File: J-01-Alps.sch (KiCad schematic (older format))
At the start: 3 parts, among them U1 ATmega32U4-AU

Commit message: Another attempt at adding more libraries
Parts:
- C5: renamed from C?; value C_Small -> 1uF; footprint (none) -> Capacitor_SMD:C_0603_1608Metric_Pad1.08x0.95mm_HandSolder
- R6: footprint Resistor_SMD:R_0402_1005Metric_Pad0.72x0.64mm_HandSolder -> Resistor_SMD:R_0603_1608Metric_Pad0.98x0.95mm_HandSolder
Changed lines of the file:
@@
 F 0 "R6" V 6454 3750 50  0000 C CNN
 F 1 "10k" V 6545 3750 50  0000 C CNN
-F 2 "Resistor_SMD:R_0402_1005Metric_Pad0.72x0.64mm_HandSolder" H 6650 3750 50  0001 C CNN
+F 2 "Resistor_SMD:R_0603_1608Metric_Pad0.98x0.95mm_HandSolder" H 6650 3750 50  0001 C CNN
 F 3 "~" H 6650 3750 50  0001 C CNN
 	1    6650 3750
@@
 	5400 4950 5500 4950
 $Comp
-L Device:C_Small C?
+L Device:C_Small C5
 U 1 1 61BC454C
 P 4200 3050
-F 0 "C?" H 4292 3096 50  0000 L CNN
-F 1 "C_Small" H 4292 3005 50  0000 L CNN
-F 2 "" H 4200 3050 50  0001 C CNN
+F 0 "C5" H 4292 3096 50  0000 L CNN
+F 1 "1uF" H 4292 3005 50  0000 L CNN
+F 2 "Capacitor_SMD:C_0603_1608Metric_Pad1.08x0.95mm_HandSolder" H 4200 3050 50  0001 C CNN
 F 3 "~" H 4200 3050 50  0001 C CNN
 	1    4200 3050

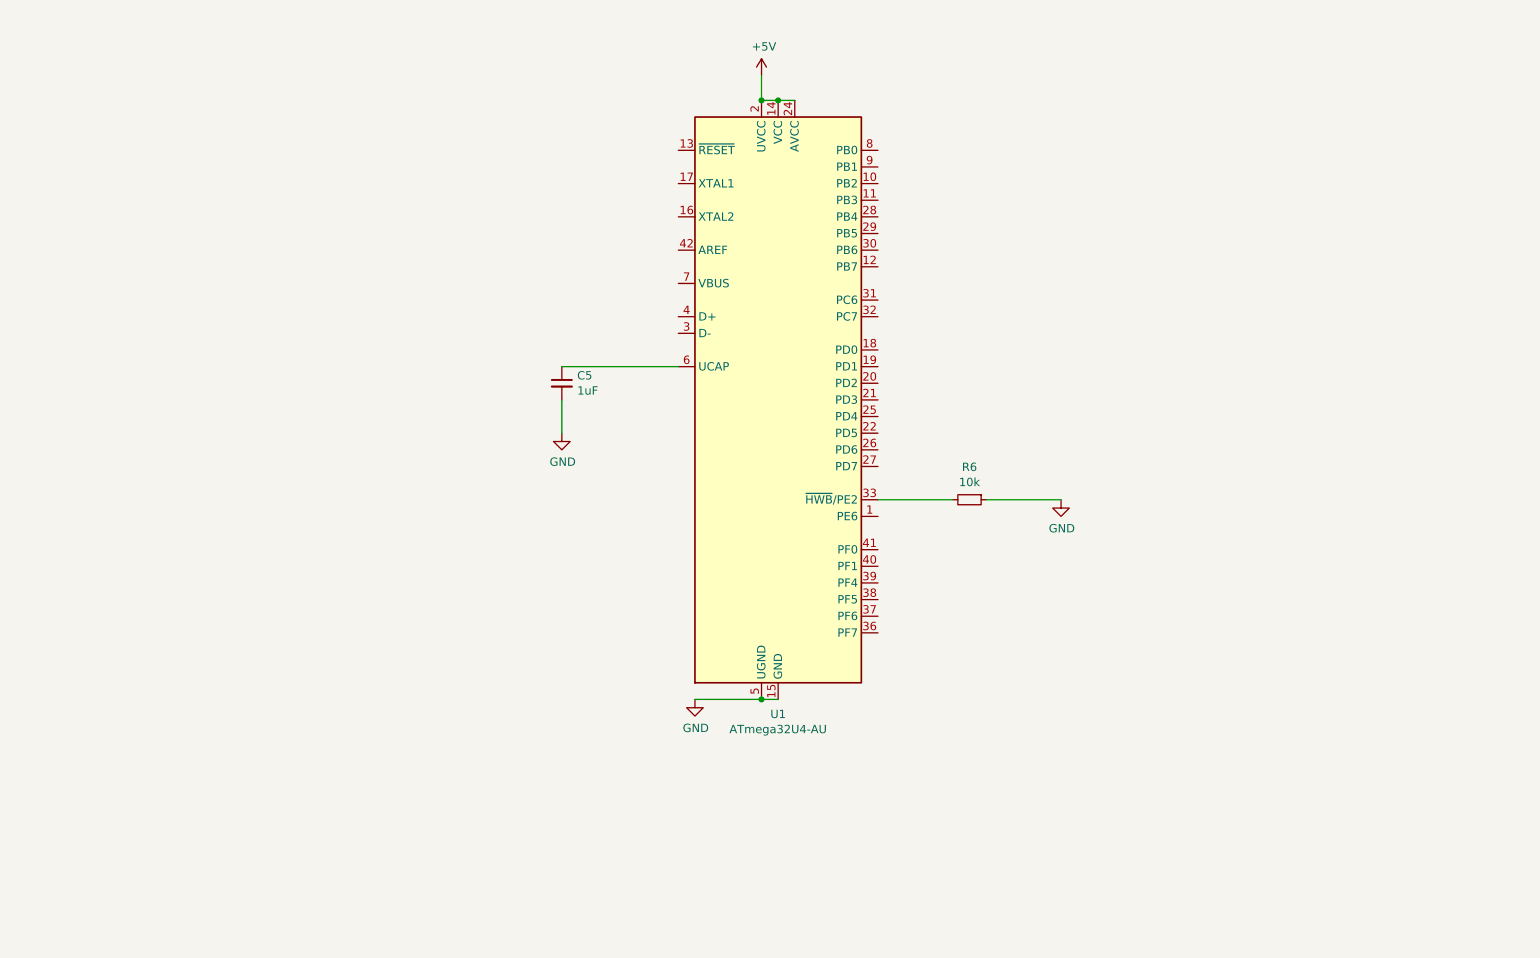
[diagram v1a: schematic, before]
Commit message: MCU and Matrix Layout
Continued work on the MCU component layout and the switch matrix.
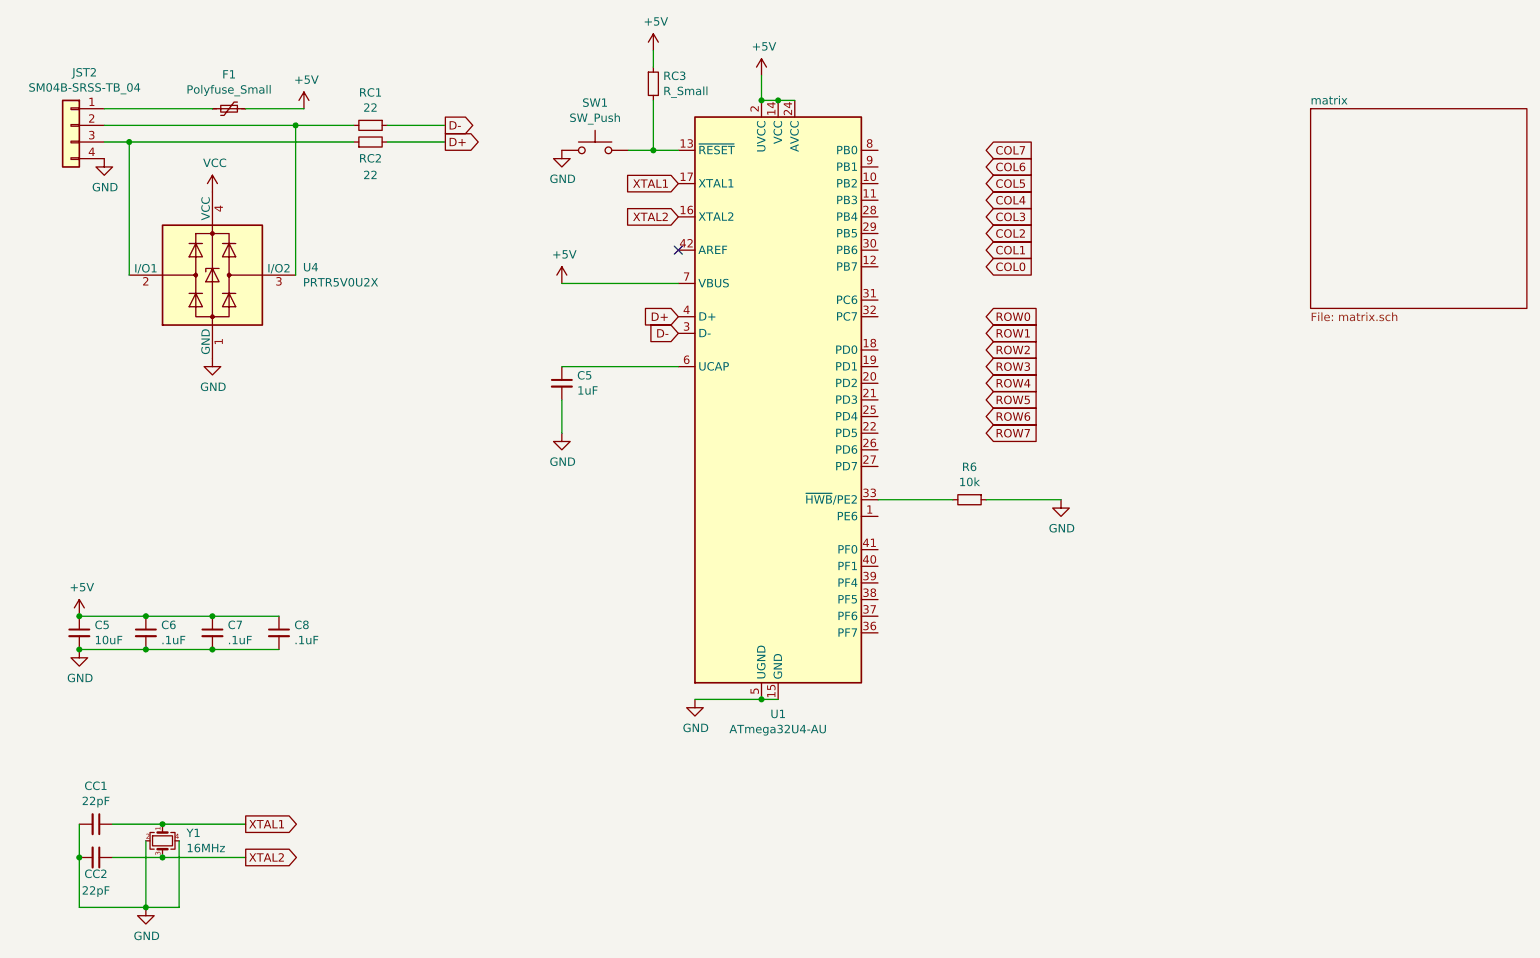
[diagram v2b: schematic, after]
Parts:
- added C5: 10uF, Capacitor_SMD:C_0603_1608Metric_Pad1.08x0.95mm_HandSolder, symbol Device:C_Small
- added C6, C7, C8: .1uF, Capacitor_SMD:C_0603_1608Metric_Pad1.08x0.95mm_HandSolder, symbol Device:C_Small
- added CC1, CC2: 22pF, Capacitor_SMD:C_0603_1608Metric_Pad1.08x0.95mm_HandSolder, symbol Device:C_Small
- added F1: Polyfuse_Small, Fuse:Fuse_1206_3216Metric_Pad1.42x1.75mm_HandSolder, symbol Device:Polyfuse_Small
- added JST2: SM04B-SRSS-TB_04, Connector_JST:JST_SH_SM04B-SRSS-TB_1x04-1MP_P1.00mm_Horizontal, symbol Connector_Generic:Conn_01x04
- added RC1, RC2: 22, Resistor_SMD:R_0603_1608Metric_Pad0.98x0.95mm_HandSolder, symbol Device:R_Small
- added RC3: R_Small, Resistor_SMD:R_0603_1608Metric_Pad0.98x0.95mm_HandSolder, symbol Device:R_Small
- added SW1: SW_Push, random-keyboard-parts:SKQGADE010, symbol Switch:SW_Push
- added U4: PRTR5V0U2X, Package_TO_SOT_SMD:SOT-143, symbol Power_Protection:PRTR5V0U2X
- added Y1: 16MHz, Crystal:Crystal_SMD_3225-4Pin_3.2x2.5mm_HandSoldering, symbol Device:Crystal_GND24_Small
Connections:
- net +5V: now also U1.7 (VBUS), C5.1, C6.1, C7.1, C8.1, F1.1, RC3.1
- net GND: now also C5.2, C6.2, C7.2, C8.2, CC1.2, CC2.2, JST2.4 (Pin_4), SW1.1, U4.1 (GND), Y1.2, Y1.4
- net at U1.13 (~RESET): now also RC3.2, SW1.2
- net XTAL2: now reaches U1.16 (XTAL2)
- net XTAL2: now also CC2.1, Y1.3
- net XTAL1: now reaches U1.17 (XTAL1)
- net XTAL1: now also CC1.1, Y1.1
- net D-: now reaches U1.3 (D-)
- net D-: now also RC1.1
- net D+: now reaches U1.4 (D+)
- net D+: now also RC2.2
- new net: F1.2, JST2.1 (Pin_1)
- new net: JST2.2 (Pin_2), RC1.2, U4.3 (I/O2)
- new net: JST2.3 (Pin_3), RC2.1, U4.2 (I/O1)
- new net VCC: U4.4 (VCC)
- no-connect marks 0 -> 1

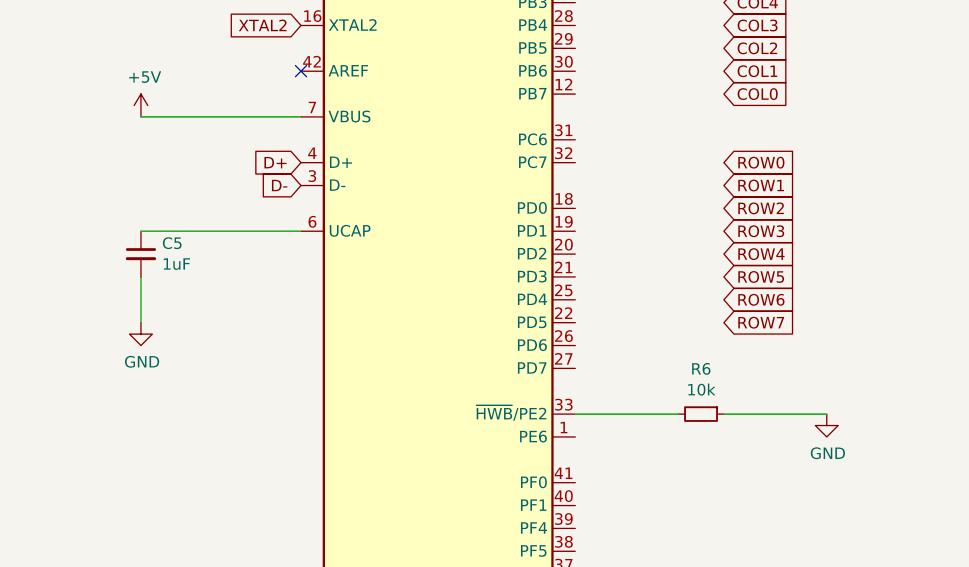
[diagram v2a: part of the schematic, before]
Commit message: Matrix Draft complete
First draft of the switch matrix is complete.
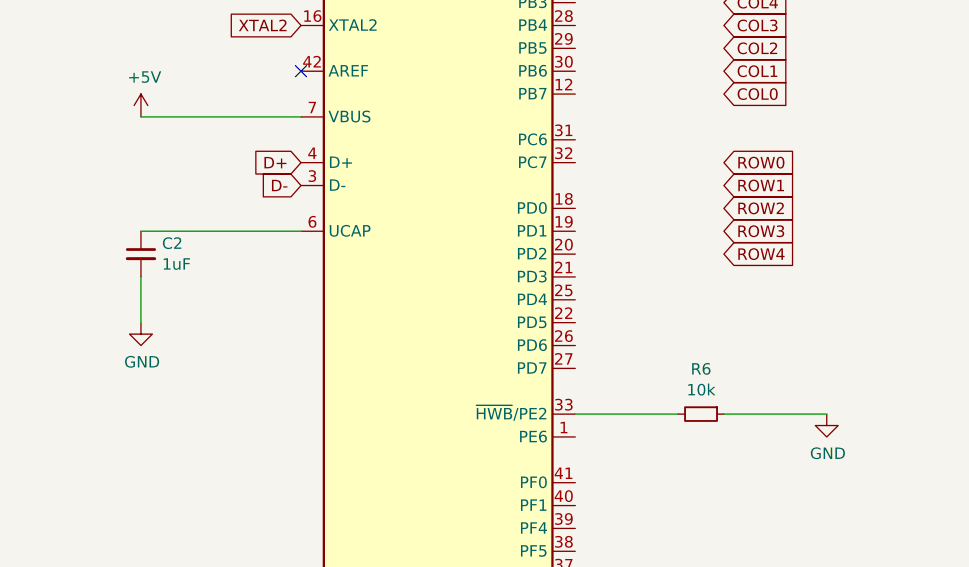
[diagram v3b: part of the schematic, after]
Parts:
- renumbered C5 to C2
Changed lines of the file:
@@
 $EndComp
 $Comp
-L power:+5V #PWR?
+L power:+5V #PWR0101
 U 1 1 61BC16E3
 P 5400 1200
-F 0 "#PWR?" H 5400 1050 50  0001 C CNN
+F 0 "#PWR0101" H 5400 1050 50  0001 C CNN
 F 1 "+5V" H 5415 1373 50  0000 C CNN
 F 2 "" H 5400 1200 50  0001 C CNN
@@
 	6100 3750 6550 3750
 $Comp
-L power:GND #PWR?
+L power:GND #PWR0102
 U 1 1 61BC3609
 P 7200 3750
-F 0 "#PWR?" H 7200 3500 50  0001 C CNN
+F 0 "#PWR0102" H 7200 3500 50  0001 C CNN
 F 1 "GND" H 7205 3577 50  0000 C CNN
 F 2 "" H 7200 3750 50  0001 C CNN
@@
 	6750 3750 7200 3750
 $Comp
-L power:GND #PWR?
+L power:GND #PWR0103
 U 1 1 61BC3DB0
 P 5000 4950
-F 0 "#PWR?" H 5000 4700 50  0001 C CNN
+F 0 "#PWR0103" H 5000 4700 50  0001 C CNN
 F 1 "GND" H 5005 4777 50  0000 C CNN
 F 2 "" H 5000 4950 50  0001 C CNN
@@
 	5400 4950 5500 4950
 $Comp
-L Device:C_Small C5
+L Device:C_Small C2
 U 1 1 61BC454C
 P 4200 3050
-F 0 "C5" H 4292 3096 50  0000 L CNN
+F 0 "C2" H 4292 3096 50  0000 L CNN
 F 1 "1uF" H 4292 3005 50  0000 L CNN
 F 2 "Capacitor_SMD:C_0603_1608Metric_Pad1.08x0.95mm_HandSolder" H 4200 3050 50  0001 C CNN
@@
 	4200 2950 4900 2950
 $Comp
-L power:GND #PWR?
+L power:GND #PWR0104
 U 1 1 61BC5372
 P 4200 3350
-F 0 "#PWR?" H 4200 3100 50  0001 C CNN
+F 0 "#PWR0104" H 4200 3100 50  0001 C CNN
 F 1 "GND" H 4205 3177 50  0000 C CNN
 F 2 "" H 4200 3350 50  0001 C CNN
@@
 D-
 $Comp
-L power:+5V #PWR?
+L power:+5V #PWR0105
 U 1 1 61BD316B
 P 4200 2450
-F 0 "#PWR?" H 4200 2300 50  0001 C CNN
+F 0 "#PWR0105" H 4200 2300 50  0001 C CNN
 F 1 "+5V" H 4215 2623 50  0000 C CNN
 F 2 "" H 4200 2450 50  0001 C CNN
@@
 $EndComp
 $Comp
-L power:GND #PWR?
+L power:GND #PWR0106
 U 1 1 61BD5C0D
 P 4200 1650
-F 0 "#PWR?" H 4200 1400 50  0001 C CNN
+F 0 "#PWR0106" H 4200 1400 50  0001 C CNN
 F 1 "GND" H 4205 1477 50  0000 C CNN
 F 2 "" H 4200 1650 50  0001 C CNN
@@
 	4750 1650 4900 1650
 $Comp
-L power:+5V #PWR?
+L power:+5V #PWR0107
 U 1 1 61BD7131
 P 4750 1050
-F 0 "#PWR?" H 4750 900 50  0001 C CNN
+F 0 "#PWR0107" H 4750 900 50  0001 C CNN
 F 1 "+5V" H 4765 1223 50  0000 C CNN
 F 2 "" H 4750 1050 50  0001 C CNN
@@
 $EndComp
 $Comp
-L power:GND #PWR?
+L power:GND #PWR0108
 U 1 1 61BDB16D
 P 1700 6200
-F 0 "#PWR?" H 1700 5950 50  0001 C CNN
+F 0 "#PWR0108" H 1700 5950 50  0001 C CNN
 F 1 "GND" H 1705 6027 50  0000 C CNN
 F 2 "" H 1700 6200 50  0001 C CNN
@@
 $EndComp
 $Comp
-L power:+5V #PWR?
+L power:+5V #PWR0109
 U 1 1 61BDFF00
 P 1300 4450
-F 0 "#PWR?" H 1300 4300 50  0001 C CNN
+F 0 "#PWR0109" H 1300 4300 50  0001 C CNN
 F 1 "+5V" H 1315 4623 50  0000 C CNN
 F 2 "" H 1300 4450 50  0001 C CNN
@@
 $EndComp
 $Comp
-L power:GND #PWR?
+L power:GND #PWR0110
 U 1 1 61BE07B1
 P 1300 4650
-F 0 "#PWR?" H 1300 4400 50  0001 C CNN
+F 0 "#PWR0110" H 1300 4400 50  0001 C CNN
 F 1 "GND" H 1305 4477 50  0000 C CNN
 F 2 "" H 1300 4650 50  0001 C CNN
@@
 	2100 4450 2500 4450
 $Comp
-L power:+5V #PWR?
+L power:+5V #PWR0111
 U 1 1 61BE4541
 P 2650 1400
-F 0 "#PWR?" H 2650 1250 50  0001 C CNN
+F 0 "#PWR0111" H 2650 1250 50  0001 C CNN
 F 1 "+5V" H 2665 1573 50  0000 C CNN
 F 2 "" H 2650 1400 50  0001 C CNN
@@
 	1450 1500 2600 1500
 $Comp
-L power:GND #PWR?
+L power:GND #PWR0112
 U 1 1 61BE8603
 P 1450 1700
-F 0 "#PWR?" H 1450 1450 50  0001 C CNN
+F 0 "#PWR0112" H 1450 1450 50  0001 C CNN
 F 1 "GND" H 1455 1527 50  0000 C CNN
 F 2 "" H 1450 1700 50  0001 C CNN
@@
 $EndComp
 $Comp
-L power:GND #PWR?
+L power:GND #PWR0113
 U 1 1 61BE9C36
 P 2100 2900
-F 0 "#PWR?" H 2100 2650 50  0001 C CNN
+F 0 "#PWR0113" H 2100 2650 50  0001 C CNN
 F 1 "GND" H 2105 2727 50  0000 C CNN
 F 2 "" H 2100 2900 50  0001 C CNN
@@
 	2600 1500 2950 1500
 $Comp
-L power:VCC #PWR?
+L power:VCC #PWR0114
 U 1 1 61BEE6C5
 P 2100 1900
-F 0 "#PWR?" H 2100 1750 50  0001 C CNN
+F 0 "#PWR0114" H 2100 1750 50  0001 C CNN
 F 1 "VCC" H 2115 2073 50  0000 C CNN
 F 2 "" H 2100 1900 50  0001 C CNN
@@
 Text GLabel 6750 3050 2    50   Input ~ 0
 ROW4
-Text GLabel 6750 3150 2    50   Input ~ 0
-ROW5
-Text GLabel 6750 3250 2    50   Input ~ 0
-ROW6
-Text GLabel 6750 3350 2    50   Input ~ 0
-ROW7
 Text GLabel 6750 2350 2    50   Input ~ 0
 COL0

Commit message: Bugfixes
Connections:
- net COL0: now also U1.9 (PB1)
- net COL1: now also U1.41 (PF0)
- net COL2: now also U1.36 (PF7)
- net COL3: now also U1.40 (PF1)
- net COL4: now also U1.39 (PF4)
- net COL5: now also U1.32 (PC7)
- net COL6: now also U1.31 (PC6)
- net COL7: now also U1.30 (PB6)
- net ROW0: now also U1.11 (PB3)
- net ROW1: now also U1.10 (PB2)
- net ROW2: now also U1.8 (PB0)
- net ROW3: now also U1.37 (PF6)
- net ROW4: now also U1.38 (PF5)
- net VCC: now also F1.2, JST2.1 (Pin_1)
- net COL17: now reaches U1.18 (PD0)
- net COL16: now reaches U1.19 (PD1)
- net COL15: now reaches U1.20 (PD2)
- net COL14: now reaches U1.21 (PD3)
- net COL13: now reaches U1.22 (PD5)
- net COL12: now reaches U1.25 (PD4)
- net COL11: now reaches U1.26 (PD6)
- net COL10: now reaches U1.27 (PD7)
- net COL9: now reaches U1.28 (PB4)
- net COL8: now reaches U1.29 (PB5)
- no-connect marks 1 -> 3
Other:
- moved on the sheet: F1, RC1, RC2
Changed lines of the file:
@@
 L power:GND #PWR0104
 U 1 1 61BC5372
-P 4200 3350
-F 0 "#PWR0104" H 4200 3100 50  0001 C CNN
-F 1 "GND" H 4205 3177 50  0000 C CNN
-F 2 "" H 4200 3350 50  0001 C CNN
-F 3 "" H 4200 3350 50  0001 C CNN
-	1    4200 3350
-	1    0    0    -1
-$EndComp
-Wire Wire Line
-	4200 3350 4200 3150
+P 4200 3300
+F 0 "#PWR0104" H 4200 3050 50  0001 C CNN
+F 1 "GND" H 4205 3127 50  0000 C CNN
+F 2 "" H 4200 3300 50  0001 C CNN
+F 3 "" H 4200 3300 50  0001 C CNN
+	1    4200 3300
+	1    0    0    -1
+$EndComp
 $Comp
 L Connector_Generic:Conn_01x04 JST2
@@
 L Device:Polyfuse_Small F1
 U 1 1 61BC3615
-P 2200 1400
-F 0 "F1" V 1995 1400 50  0000 C CNN
-F 1 "Polyfuse_Small" V 2086 1400 50  0000 C CNN
-F 2 "Fuse:Fuse_1206_3216Metric_Pad1.42x1.75mm_HandSolder" H 2250 1200 50  0001 L CNN
-F 3 "~" H 2200 1400 50  0001 C CNN
-	1    2200 1400
+P 1750 3700
+F 0 "F1" V 1545 3700 50  0000 C CNN
+F 1 "Polyfuse_Small" V 1636 3700 50  0000 C CNN
+F 2 "Fuse:Fuse_1206_3216Metric_Pad1.42x1.75mm_HandSolder" H 1800 3500 50  0001 L CNN
+F 3 "~" H 1750 3700 50  0001 C CNN
+	1    1750 3700
 	0    1    1    0
 $EndComp
@@
 L Device:R_Small RC1
 U 1 1 61BC52CD
-P 3050 1500
-F 0 "RC1" V 2854 1500 50  0000 C CNN
-F 1 "22" V 2945 1500 50  0000 C CNN
-F 2 "Resistor_SMD:R_0603_1608Metric_Pad0.98x0.95mm_HandSolder" H 3050 1500 50  0001 C CNN
-F 3 "~" H 3050 1500 50  0001 C CNN
-	1    3050 1500
+P 3000 1500
+F 0 "RC1" V 2804 1500 50  0000 C CNN
+F 1 "22" V 2895 1500 50  0000 C CNN
+F 2 "Resistor_SMD:R_0603_1608Metric_Pad0.98x0.95mm_HandSolder" H 3000 1500 50  0001 C CNN
+F 3 "~" H 3000 1500 50  0001 C CNN
+	1    3000 1500
 	0    1    1    0
 $EndComp
@@
 L Device:R_Small RC2
 U 1 1 61BC5632
-P 3050 1600
-F 0 "RC2" V 2950 1600 50  0000 C CNN
-F 1 "22" V 2850 1600 50  0000 C CNN
-F 2 "Resistor_SMD:R_0603_1608Metric_Pad0.98x0.95mm_HandSolder" H 3050 1600 50  0001 C CNN
-F 3 "~" H 3050 1600 50  0001 C CNN
-	1    3050 1600
+P 3000 1600
+F 0 "RC2" V 2900 1600 50  0000 C CNN
+F 1 "22" V 2800 1600 50  0000 C CNN
+F 2 "Resistor_SMD:R_0603_1608Metric_Pad0.98x0.95mm_HandSolder" H 3000 1600 50  0001 C CNN
+F 3 "~" H 3000 1600 50  0001 C CNN
+	1    3000 1600
 	0    -1   -1   0
 $EndComp
-Text GLabel 3500 1500 2    50   Output ~ 0
+Text GLabel 3300 1500 2    50   Output ~ 0
 D-
-Text GLabel 3500 1600 2    50   Output ~ 0
+Text GLabel 3300 1600 2    50   Output ~ 0
 D+
 Wire Wire Line
-	3150 1500 3500 1500
-Wire Wire Line
-	3150 1600 3500 1600
+	3100 1500 3300 1500
+Wire Wire Line
+	3100 1600 3300 1600
 Text GLabel 4900 2650 0    50   Input ~ 0
 D+
@@
 L power:+5V #PWR0111
 U 1 1 61BE4541
-P 2650 1400
-F 0 "#PWR0111" H 2650 1250 50  0001 C CNN
-F 1 "+5V" H 2665 1573 50  0000 C CNN
-F 2 "" H 2650 1400 50  0001 C CNN
-F 3 "" H 2650 1400 50  0001 C CNN
-	1    2650 1400
-	1    0    0    -1
-$EndComp
-Wire Wire Line
-	2300 1400 2650 1400
+P 2150 3700
+F 0 "#PWR0111" H 2150 3550 50  0001 C CNN
+F 1 "+5V" H 2165 3873 50  0000 C CNN
+F 2 "" H 2150 3700 50  0001 C CNN
+F 3 "" H 2150 3700 50  0001 C CNN
+	1    2150 3700
+	1    0    0    -1
+$EndComp
+Wire Wire Line
+	1850 3700 2150 3700
 Wire Wire Line
 	1450 1500 2600 1500
@@
 Connection ~ 1600 1600
 Wire Wire Line
-	1600 1600 2950 1600
+	1600 1600 2900 1600
 Wire Wire Line
 	2600 2400 2600 1500
 Connection ~ 2600 1500
 Wire Wire Line
-	2600 1500 2950 1500
-$Comp
-L power:VCC #PWR0114
-U 1 1 61BEE6C5
-P 2100 1900
-F 0 "#PWR0114" H 2100 1750 50  0001 C CNN
-F 1 "VCC" H 2115 2073 50  0000 C CNN
-F 2 "" H 2100 1900 50  0001 C CNN
-F 3 "" H 2100 1900 50  0001 C CNN
-	1    2100 1900
-	1    0    0    -1
-$EndComp
+	2600 1500 2900 1500
 $Sheet
 S 8700 1400 1300 1200
@@
 F1 "matrix.sch" 50
 $EndSheet
-Text GLabel 6750 2650 2    50   Input ~ 0
+Text GLabel 6100 1950 2    50   Input ~ 0
 ROW0
-Text GLabel 6750 2750 2    50   Input ~ 0
+Text GLabel 6100 1850 2    50   Input ~ 0
 ROW1
-Text GLabel 6750 2850 2    50   Input ~ 0
+Text GLabel 6100 1650 2    50   Input ~ 0
 ROW2
-Text GLabel 6750 2950 2    50   Input ~ 0
+Text GLabel 6100 4450 2    50   Input ~ 0
 ROW3
-Text GLabel 6750 3050 2    50   Input ~ 0
+Text GLabel 6100 4350 2    50   Input ~ 0
 ROW4
-Text GLabel 6750 2350 2    50   Input ~ 0
+Text GLabel 6100 1750 2    50   Input ~ 0
 COL0
-Text GLabel 6750 2250 2    50   Input ~ 0
+Text GLabel 6100 4050 2    50   Input ~ 0
 COL1
-Text GLabel 6750 2150 2    50   Input ~ 0
+Text GLabel 6100 4550 2    50   Input ~ 0
 COL2
-Text GLabel 6750 2050 2    50   Input ~ 0
+Text GLabel 6100 4150 2    50   Input ~ 0
 COL3
-Text GLabel 6750 1950 2    50   Input ~ 0
+Text GLabel 6100 4250 2    50   Input ~ 0
 COL4
-Text GLabel 6750 1850 2    50   Input ~ 0
+Text GLabel 6100 2650 2    50   Input ~ 0
 COL5
-Text GLabel 6750 1750 2    50   Input ~ 0
+Text GLabel 6100 2550 2    50   Input ~ 0
 COL6
-Text GLabel 6750 1650 2    50   Input ~ 0
+Text GLabel 6100 2250 2    50   Input ~ 0
 COL7
-Wire Wire Line
-	1450 1400 2100 1400
+Text GLabel 6100 2150 2    50   Input ~ 0
+COL8
+Text GLabel 6100 3450 2    50   Input ~ 0
+COL11
+Text GLabel 6100 3350 2    50   Input ~ 0
+COL13
+Text GLabel 6100 3250 2    50   Input ~ 0
+COL12
+Text GLabel 6100 2050 2    50   Input ~ 0
+COL9
+Text GLabel 6100 3550 2    50   Input ~ 0
+COL10
+Text GLabel 6100 3150 2    50   Input ~ 0
+COL14
+Text GLabel 6100 3050 2    50   Input ~ 0
+COL15
+Text GLabel 6100 2950 2    50   Input ~ 0
+COL16
+Text GLabel 6100 2850 2    50   Input ~ 0
+COL17
+NoConn ~ 6100 3850
+NoConn ~ 6100 2350
+$Comp
+L power:VCC #PWR0114
+U 1 1 61F1803F
+P 1300 3700
+F 0 "#PWR0114" H 1300 3550 50  0001 C CNN
+F 1 "VCC" H 1315 3873 50  0000 C CNN
+F 2 "" H 1300 3700 50  0001 C CNN
+F 3 "" H 1300 3700 50  0001 C CNN
+	1    1300 3700
+	1    0    0    -1
+$EndComp
+Wire Wire Line
+	1300 3700 1650 3700
+$Comp
+L power:VCC #PWR0115
+U 1 1 61F1B227
+P 2000 1400
+F 0 "#PWR0115" H 2000 1250 50  0001 C CNN
+F 1 "VCC" H 2015 1573 50  0000 C CNN
+F 2 "" H 2000 1400 50  0001 C CNN
+F 3 "" H 2000 1400 50  0001 C CNN
+	1    2000 1400
+	1    0    0    -1
+$EndComp
+Wire Wire Line
+	1450 1400 2000 1400
+$Comp
+L power:VCC #PWR0116
+U 1 1 61F1C94A
+P 2100 1900
+F 0 "#PWR0116" H 2100 1750 50  0001 C CNN
+F 1 "VCC" H 2115 2073 50  0000 C CNN
+F 2 "" H 2100 1900 50  0001 C CNN
+F 3 "" H 2100 1900 50  0001 C CNN
+	1    2100 1900
+	1    0    0    -1
+$EndComp
+Wire Wire Line
+	4200 3300 4200 3150
 $EndSCHEMATC
